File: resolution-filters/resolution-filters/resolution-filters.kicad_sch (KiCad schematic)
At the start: 55 parts, among them J501 Conn_Coaxial, J502 Terminal Block, J503 Conn_Coaxial, K501 G5V-1, K502 G5V-1, SW501 SW_SPST, T501 Transformer_1P_1S, T502 Transformer_1P_1S, Y501 10.7MHz, Y502 10.7MHz, Y503 10.7MHz, Y504 10.7MHz

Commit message: minor changes to schematic
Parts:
- added R504, R506: 10M, Resistor_THT:R_Axial_DIN0207_L6.3mm_D2.5mm_P7.62mm_Horizontal, symbol Device:R_Small_US
- added R505: 0, Resistor_THT:R_Axial_DIN0207_L6.3mm_D2.5mm_P7.62mm_Horizontal, symbol Device:R_Small_US
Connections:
- net GND: now also C524.2, R504.2, R506.2
- net at C523.2, C524.1: now also R505.2, R506.1
- net at K502.1: now also R504.1, R505.1; no longer C524.2
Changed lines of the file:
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@@
   (junction (at 166.37 61.595) (diameter 0) (color 0 0 0 0)
   )
+  (junction (at 252.73 152.4) (diameter 0) (color 0 0 0 0)
+  )
   (junction (at 53.34 61.595) (diameter 0) (color 0 0 0 0)
   )
+  (junction (at 238.76 152.4) (diameter 0) (color 0 0 0 0)
+  )
+  (junction (at 252.73 77.47) (diameter 0) (color 0 0 0 0)
+  )
   (junction (at 240.03 61.595) (diameter 0) (color 0 0 0 0)
   )
@@
     (stroke (width 0) (type default) (color 0 0 0 0))
   )
+  (wire (pts (xy 252.73 92.075) (xy 252.73 100.33))
+    (stroke (width 0) (type default) (color 0 0 0 0))
+  )
   (wire (pts (xy 135.89 21.59) (xy 53.975 21.59))
     (stroke (width 0) (type default) (color 0 0 0 0))
@@
     (stroke (width 0) (type default) (color 0 0 0 0))
   )
+  (wire (pts (xy 262.89 77.47) (xy 262.89 152.4))
+    (stroke (width 0) (type default) (color 0 0 0 0))
+  )
   (wire (pts (xy 196.215 31.75) (xy 212.09 31.75))
     (stroke (width 0) (type default) (color 0 0 0 0))
@@
     (stroke (width 0) (type default) (color 0 0 0 0))
   )
+  (wire (pts (xy 248.92 152.4) (xy 252.73 152.4))
+    (stroke (width 0) (type default) (color 0 0 0 0))
+  )
   (wire (pts (xy 25.4 113.03) (xy 25.4 133.35))
     (stroke (width 0) (type default) (color 0 0 0 0))
@@
     (stroke (width 0) (type default) (color 0 0 0 0))
   )
-  (wire (pts (xy 252.73 92.075) (xy 252.73 153.035))
+  (wire (pts (xy 213.36 152.4) (xy 213.36 153.035))
     (stroke (width 0) (type default) (color 0 0 0 0))
   )
@@
     (stroke (width 0) (type default) (color 0 0 0 0))
   )
+  (wire (pts (xy 252.73 157.48) (xy 252.73 162.56))
+    (stroke (width 0) (type default) (color 0 0 0 0))
+  )
   (wire (pts (xy 100.33 160.655) (xy 100.33 163.195))
     (stroke (width 0) (type default) (color 0 0 0 0))
@@
     (stroke (width 0) (type default) (color 0 0 0 0))
   )
-  (wire (pts (xy 252.73 69.215) (xy 252.73 86.995))
+  (wire (pts (xy 252.73 69.215) (xy 252.73 77.47))
     (stroke (width 0) (type default) (color 0 0 0 0))
   )
@@
     (stroke (width 0) (type default) (color 0 0 0 0))
   )
+  (wire (pts (xy 213.36 152.4) (xy 238.76 152.4))
+    (stroke (width 0) (type default) (color 0 0 0 0))
+  )
   (wire (pts (xy 80.01 113.03) (xy 72.39 113.03))
     (stroke (width 0) (type default) (color 0 0 0 0))
@@
     (stroke (width 0) (type default) (color 0 0 0 0))
   )
+  (wire (pts (xy 262.89 152.4) (xy 252.73 152.4))
+    (stroke (width 0) (type default) (color 0 0 0 0))
+  )
+  (wire (pts (xy 243.84 152.4) (xy 238.76 152.4))
+    (stroke (width 0) (type default) (color 0 0 0 0))
+  )
   (wire (pts (xy 165.735 113.665) (xy 181.61 113.665))
     (stroke (width 0) (type default) (color 0 0 0 0))
@@
     (stroke (width 0) (type default) (color 0 0 0 0))
   )
-  (wire (pts (xy 213.36 153.035) (xy 252.73 153.035))
-    (stroke (width 0) (type default) (color 0 0 0 0))
-  )
   (wire (pts (xy 233.68 113.665) (xy 233.68 147.955))
     (stroke (width 0) (type default) (color 0 0 0 0))
   )
+  (wire (pts (xy 238.76 157.48) (xy 238.76 162.56))
+    (stroke (width 0) (type default) (color 0 0 0 0))
+  )
   (wire (pts (xy 43.815 21.59) (xy 40.64 21.59))
     (stroke (width 0) (type default) (color 0 0 0 0))
@@
     (stroke (width 0) (type default) (color 0 0 0 0))
   )
+  (wire (pts (xy 252.73 77.47) (xy 252.73 86.995))
+    (stroke (width 0) (type default) (color 0 0 0 0))
+  )
   (wire (pts (xy 65.405 150.495) (xy 51.435 150.495))
     (stroke (width 0) (type default) (color 0 0 0 0))
@@
   )
   (wire (pts (xy 181.61 113.665) (xy 181.61 118.11))
+    (stroke (width 0) (type default) (color 0 0 0 0))
+  )
+  (wire (pts (xy 252.73 77.47) (xy 262.89 77.47))
     (stroke (width 0) (type default) (color 0 0 0 0))
   )
@@
     )
     (pin "1")
+  )
+  (symbol (lib_id "Device:R_Small_US") (at 238.76 154.94 0) (unit 1)
+    (in_bom yes) (on_board yes) (fields_autoplaced)
+    (property "Reference" "R504" (id 0) (at 241.3 153.6699 0)
+      (effects (font (size 1.27 1.27)) (justify left))
+    )
+    (property "Value" "10M" (id 1) (at 241.3 156.2099 0)
+      (effects (font (size 1.27 1.27)) (justify left))
+    )
+    (property "Footprint" "Resistor_THT:R_Axial_DIN0207_L6.3mm_D2.5mm_P7.62mm_Horizontal" (id 2) (at 238.76 154.94 0)
+      (effects (font (size 1.27 1.27)) hide)
+    )
+    (property "Datasheet" "https://www.yageo.com/upload/media/product/productsearch/datasheet/lr/YAGEO%20RSF_datasheet_2021v0.pdf" (id 3) (at 238.76 154.94 0)
+      (effects (font (size 1.27 1.27)) hide)
+    )
+    (pin "1")
+    (pin "2")
   )
   (symbol (lib_id "power:GND") (at 108.585 127 0) (unit 1)
@@
     (pin "2")
     (pin "3")
+  )
+  (symbol (lib_id "power:GND") (at 252.73 100.33 0) (unit 1)
+    (in_bom yes) (on_board yes) (fields_autoplaced)
+    (property "Reference" "#PWR?" (id 0) (at 252.73 106.68 0)
+      (effects (font (size 1.27 1.27)) hide)
+    )
+    (property "Value" "GND" (id 1) (at 252.73 105.41 0))
+    (property "Footprint" "" (id 2) (at 252.73 100.33 0)
+      (effects (font (size 1.27 1.27)) hide)
+    )
+    (property "Datasheet" "" (id 3) (at 252.73 100.33 0)
+      (effects (font (size 1.27 1.27)) hide)
+    )
+    (pin "1")
   )
   (symbol (lib_id "Device:C_Trim_Small") (at 53.34 78.105 0) (unit 1)
@@
     (pin "2")
   )
+  (symbol (lib_id "Device:R_Small_US") (at 252.73 154.94 0) (unit 1)
+    (in_bom yes) (on_board yes) (fields_autoplaced)
+    (property "Reference" "R506" (id 0) (at 255.27 153.6699 0)
+      (effects (font (size 1.27 1.27)) (justify left))
+    )
+    (property "Value" "10M" (id 1) (at 255.27 156.2099 0)
+      (effects (font (size 1.27 1.27)) (justify left))
+    )
+    (property "Footprint" "Resistor_THT:R_Axial_DIN0207_L6.3mm_D2.5mm_P7.62mm_Horizontal" (id 2) (at 252.73 154.94 0)
+      (effects (font (size 1.27 1.27)) hide)
+    )
+    (property "Datasheet" "https://www.yageo.com/upload/media/product/productsearch/datasheet/lr/YAGEO%20RSF_datasheet_2021v0.pdf" (id 3) (at 252.73 154.94 0)
+      (effects (font (size 1.27 1.27)) hide)
+    )
+    (pin "1")
+    (pin "2")
+  )
   (symbol (lib_id "Device:C_Trim_Small") (at 53.975 118.11 0) (unit 1)
     (in_bom yes) (on_board yes)
@@
     (pin "1")
   )
+  (symbol (lib_id "power:GND") (at 252.73 162.56 0) (unit 1)
+    (in_bom yes) (on_board yes) (fields_autoplaced)
+    (property "Reference" "#PWR?" (id 0) (at 252.73 168.91 0)
+      (effects (font (size 1.27 1.27)) hide)
+    )
+    (property "Value" "GND" (id 1) (at 252.73 167.64 0))
+    (property "Footprint" "" (id 2) (at 252.73 162.56 0)
+      (effects (font (size 1.27 1.27)) hide)
+    )
+    (property "Datasheet" "" (id 3) (at 252.73 162.56 0)
+      (effects (font (size 1.27 1.27)) hide)
+    )
+    (pin "1")
+  )
   (symbol (lib_id "power:GND") (at 194.31 129.54 0) (unit 1)
     (in_bom yes) (on_board yes) (fields_autoplaced)
@@
     (pin "2")
   )
+  (symbol (lib_id "Device:R_Small_US") (at 246.38 152.4 90) (unit 1)
+    (in_bom yes) (on_board yes) (fields_autoplaced)
+    (property "Reference" "R505" (id 0) (at 246.38 146.05 90))
+    (property "Value" "0" (id 1) (at 246.38 148.59 90))
+    (property "Footprint" "Resistor_THT:R_Axial_DIN0207_L6.3mm_D2.5mm_P7.62mm_Horizontal" (id 2) (at 246.38 152.4 0)
+      (effects (font (size 1.27 1.27)) hide)
+    )
+    (property "Datasheet" "https://www.yageo.com/upload/media/product/productsearch/datasheet/lr/YAGEO%20RSF_datasheet_2021v0.pdf" (id 3) (at 246.38 152.4 0)
+      (effects (font (size 1.27 1.27)) hide)
+    )
+    (pin "1")
+    (pin "2")
+  )
   (symbol (lib_id "power:GND") (at 50.165 127 0) (unit 1)
     (in_bom yes) (on_board yes) (fields_autoplaced)
@@
     (pin "1")
   )
+  (symbol (lib_id "power:GND") (at 238.76 162.56 0) (unit 1)
+    (in_bom yes) (on_board yes) (fields_autoplaced)
+    (property "Reference" "#PWR?" (id 0) (at 238.76 168.91 0)
+      (effects (font (size 1.27 1.27)) hide)
+    )
+    (property "Value" "GND" (id 1) (at 238.76 167.64 0))
+    (property "Footprint" "" (id 2) (at 238.76 162.56 0)
+      (effects (font (size 1.27 1.27)) hide)
+    )
+    (property "Datasheet" "" (id 3) (at 238.76 162.56 0)
+      (effects (font (size 1.27 1.27)) hide)
+    )
+    (pin "1")
+  )
   (symbol (lib_id "power:GND") (at 142.875 43.18 0) (unit 1)
     (in_bom yes) (on_board yes) (fields_autoplaced)
@@
       (reference "#PWR0542") (unit 1) (value "GND") (footprint "")
     )
+    (path "/35fe081f-dbbc-4b42-a7a6-8eae86c45ae6"
+      (reference "#PWR?") (unit 1) (value "GND") (footprint "")
+    )
+    (path "/813033cb-6509-476d-9f83-7f71c7a71115"
+      (reference "#PWR?") (unit 1) (value "GND") (footprint "")
+    )
+    (path "/f8f0dbab-2295-44be-ac81-7b459c89e2d0"
+      (reference "#PWR?") (unit 1) (value "GND") (footprint "")
+    )
     (path "/d652cc14-cade-40ef-aafa-a5f29bc86d85"
       (reference "C501") (unit 1) (value "56p") (footprint "Capacitor_THT:C_Disc_D5.0mm_W2.5mm_P5.00mm")
@@
       (reference "R503") (unit 1) (value "150") (footprint "Resistor_THT:R_Axial_DIN0207_L6.3mm_D2.5mm_P7.62mm_Horizontal")
     )
+    (path "/303cb82b-dbdf-496e-9073-313c41175705"
+      (reference "R504") (unit 1) (value "10M") (footprint "Resistor_THT:R_Axial_DIN0207_L6.3mm_D2.5mm_P7.62mm_Horizontal")
+    )
     (path "/6171ffef-02be-45d5-a410-63aa493274a2"
       (reference "R504") (unit 1) (value "270") (footprint "Resistor_THT:R_Axial_DIN0207_L6.3mm_D2.5mm_P7.62mm_Horizontal")
@@
       (reference "R505") (unit 1) (value "9.1k") (footprint "Resistor_THT:R_Axial_DIN0207_L6.3mm_D2.5mm_P7.62mm_Horizontal")
     )
+    (path "/ed25e332-d405-4681-a179-fd49944d313e"
+      (reference "R505") (unit 1) (value "0") (footprint "Resistor_THT:R_Axial_DIN0207_L6.3mm_D2.5mm_P7.62mm_Horizontal")
+    )
+    (path "/4b9e1409-9985-446c-aa88-d0c28c620215"
+      (reference "R506") (unit 1) (value "10M") (footprint "Resistor_THT:R_Axial_DIN0207_L6.3mm_D2.5mm_P7.62mm_Horizontal")
+    )
     (path "/a8c5b699-e167-4f68-a36e-3f11ebc2816a"

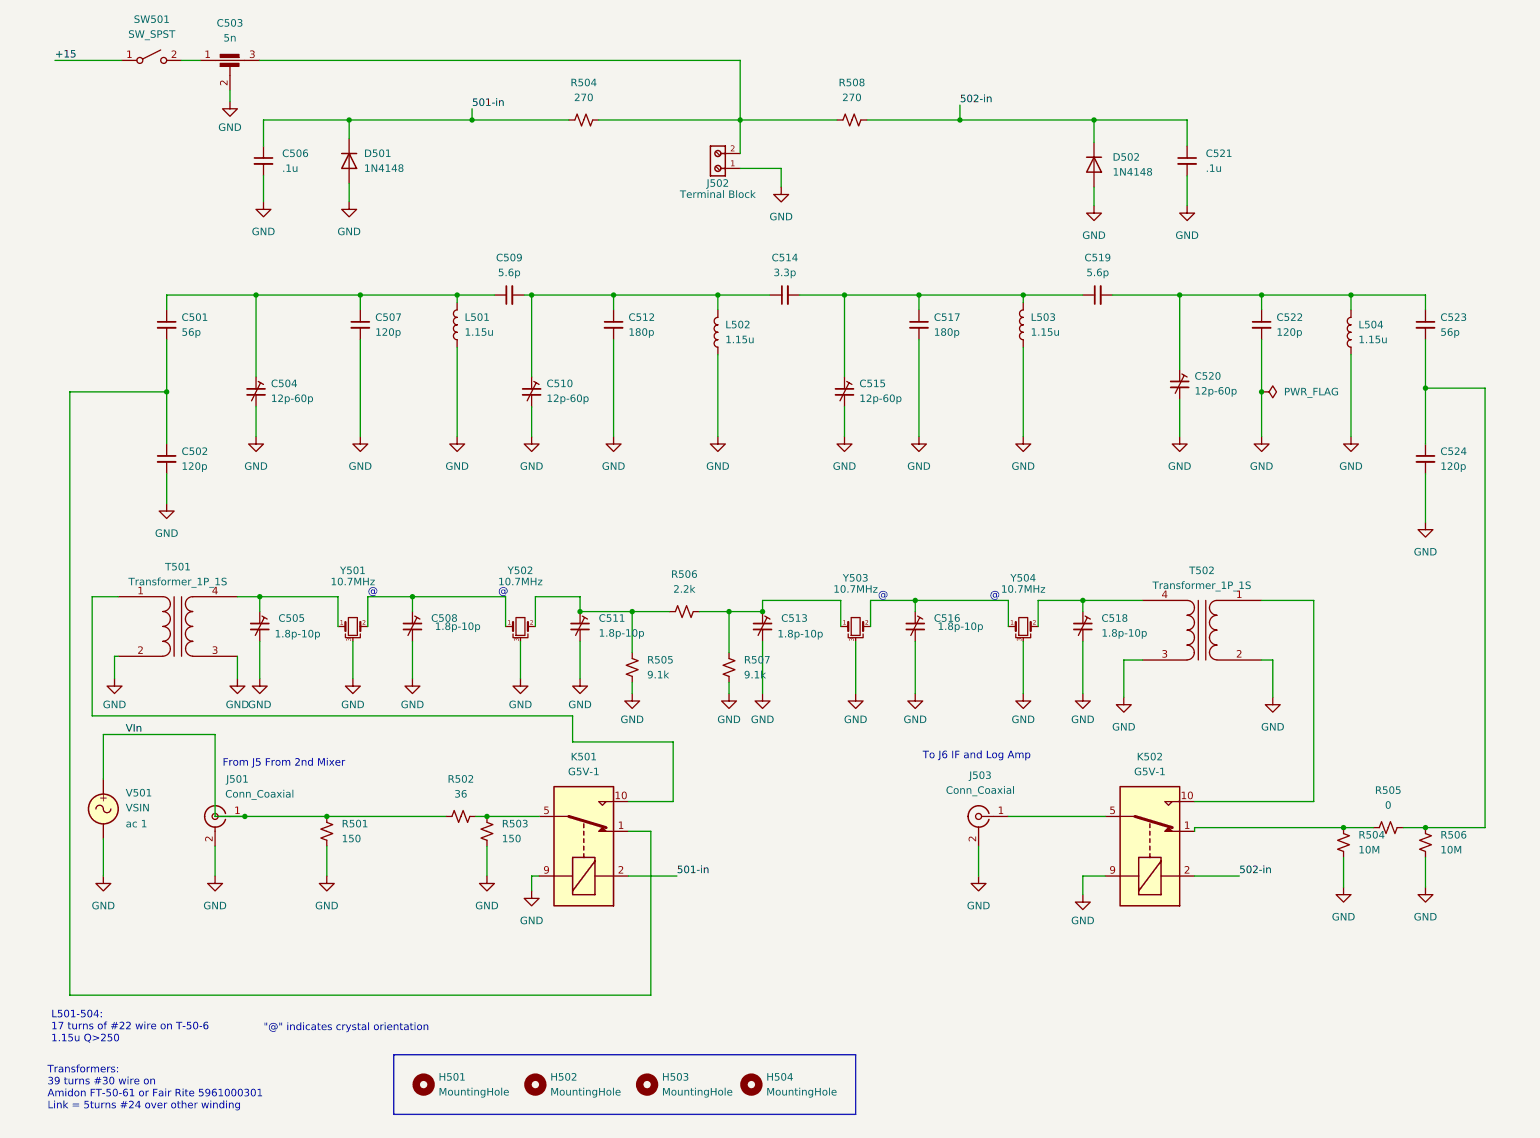
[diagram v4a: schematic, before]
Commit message: improved if and log amp and second lo/mixer
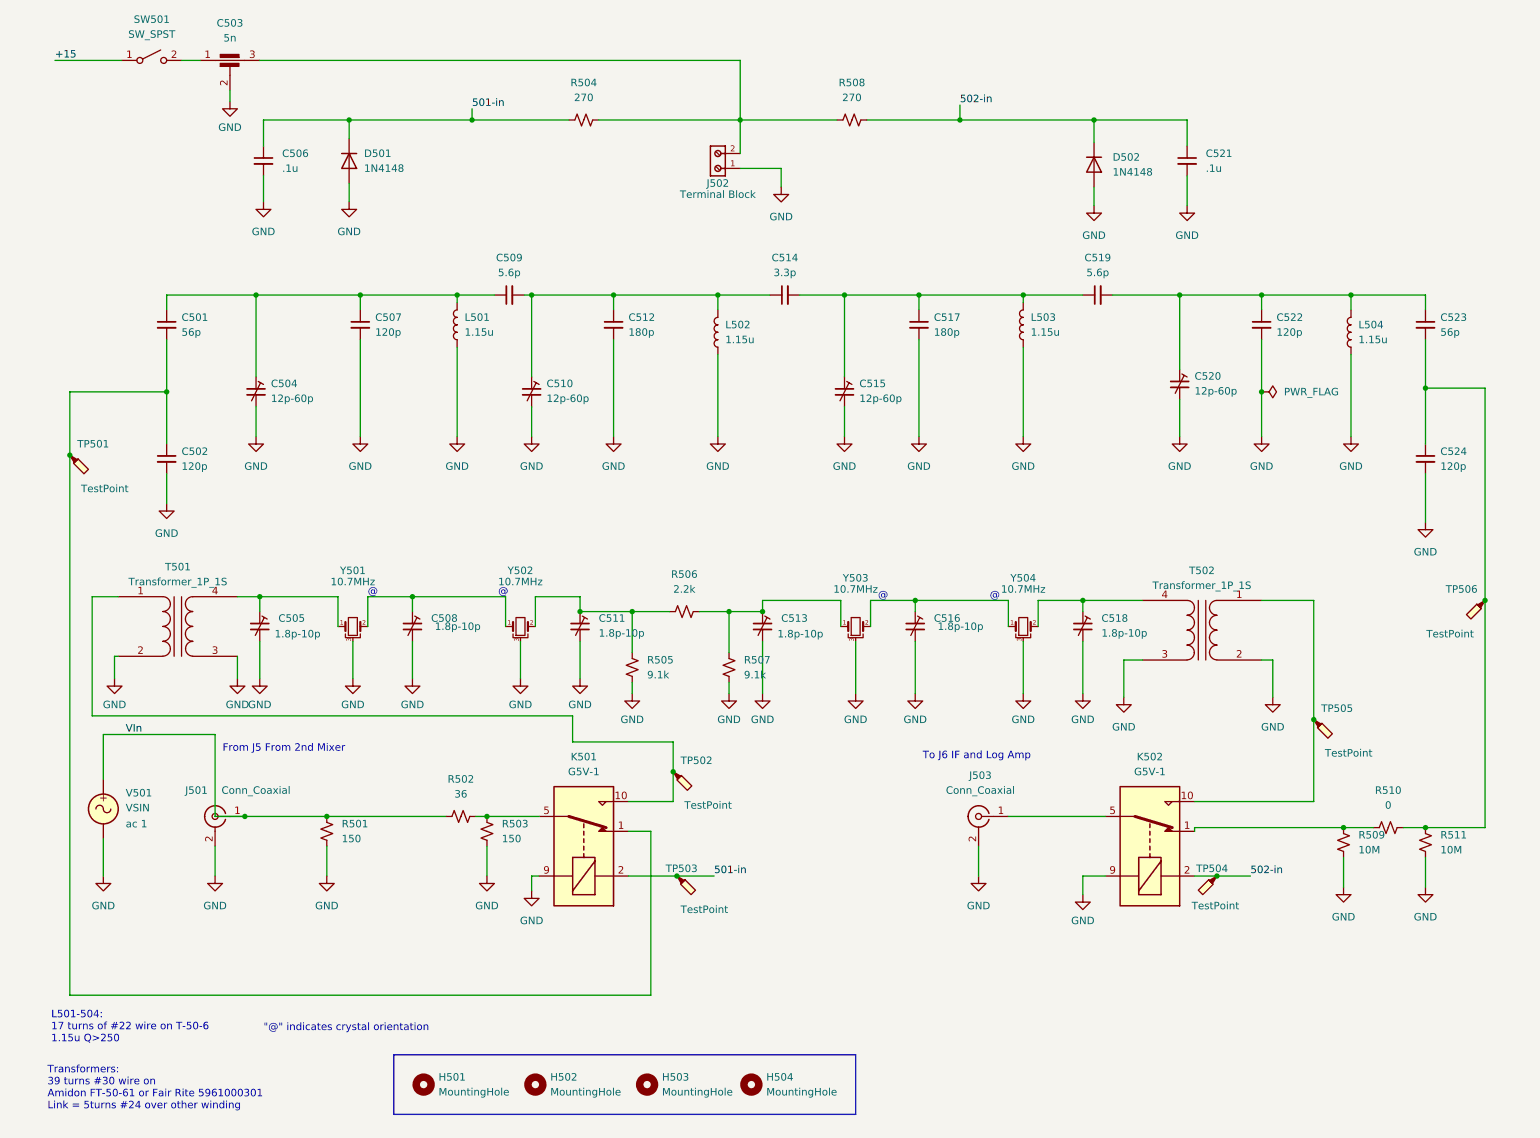
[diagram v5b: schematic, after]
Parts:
- added TP501, TP502, TP503, TP504, TP505, TP506: TestPoint, TestPoint:TestPoint_Pad_1.0x1.0mm, symbol Connector:TestPoint_Probe
- renumbered R504 to R509, R505 to R510, R506 to R511
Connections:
- net 501-in: now also TP503.1
- net 502-in: now also TP504.1
- net at K502.10, T502.1 (AA): now also TP505.1
- net at C501.2, C502.1, K501.1: now also TP501.1
- net at C523.2, C524.1, R510.2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: now also TP506.1
- net at K501.10, T501.1 (AA): now also TP502.1

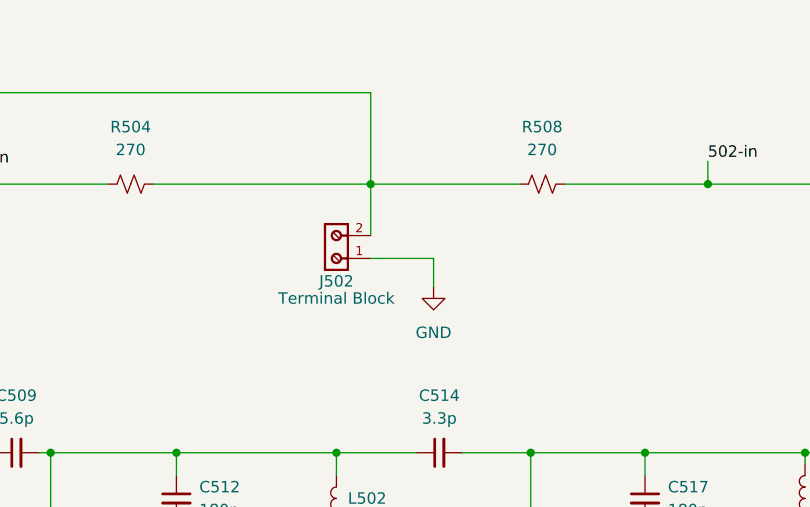
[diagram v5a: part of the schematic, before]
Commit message: resolution-filters update
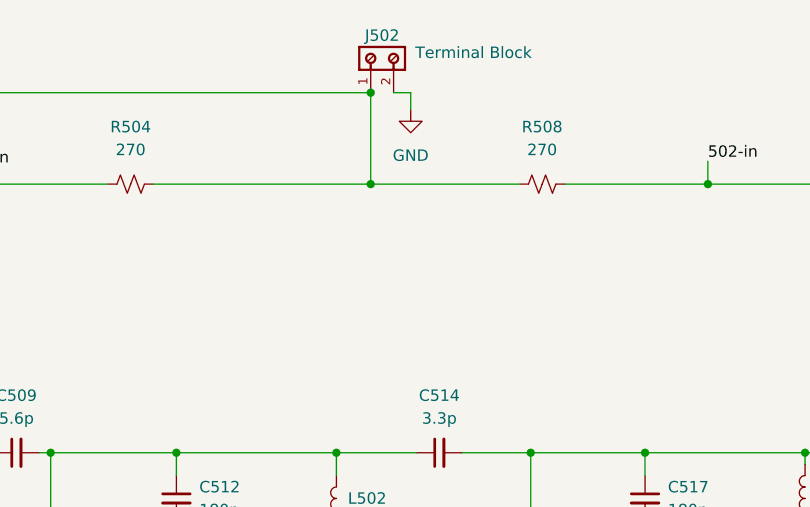
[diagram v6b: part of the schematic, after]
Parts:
- TP501, TP502, TP503, TP504, TP505, TP506: footprint TestPoint:TestPoint_Pad_1.0x1.0mm -> TestPoint:TestPoint_Pad_D2.0mm
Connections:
- net GND: now also J502.2; no longer J502.1
- net at C503.3, R504.2, R508.1: now also J502.1; no longer J502.2
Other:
- moved on the sheet: J502
